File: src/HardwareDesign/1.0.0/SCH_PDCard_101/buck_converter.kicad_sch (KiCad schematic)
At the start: 43 parts, among them IC1 TPS552882QRPMRQ1, IC4 SN74LVC1G97QDCKRQ1, IC5 SN74LVC1G97QDCKRQ1, T1 BSZ065N06, T2 BSZ065N06

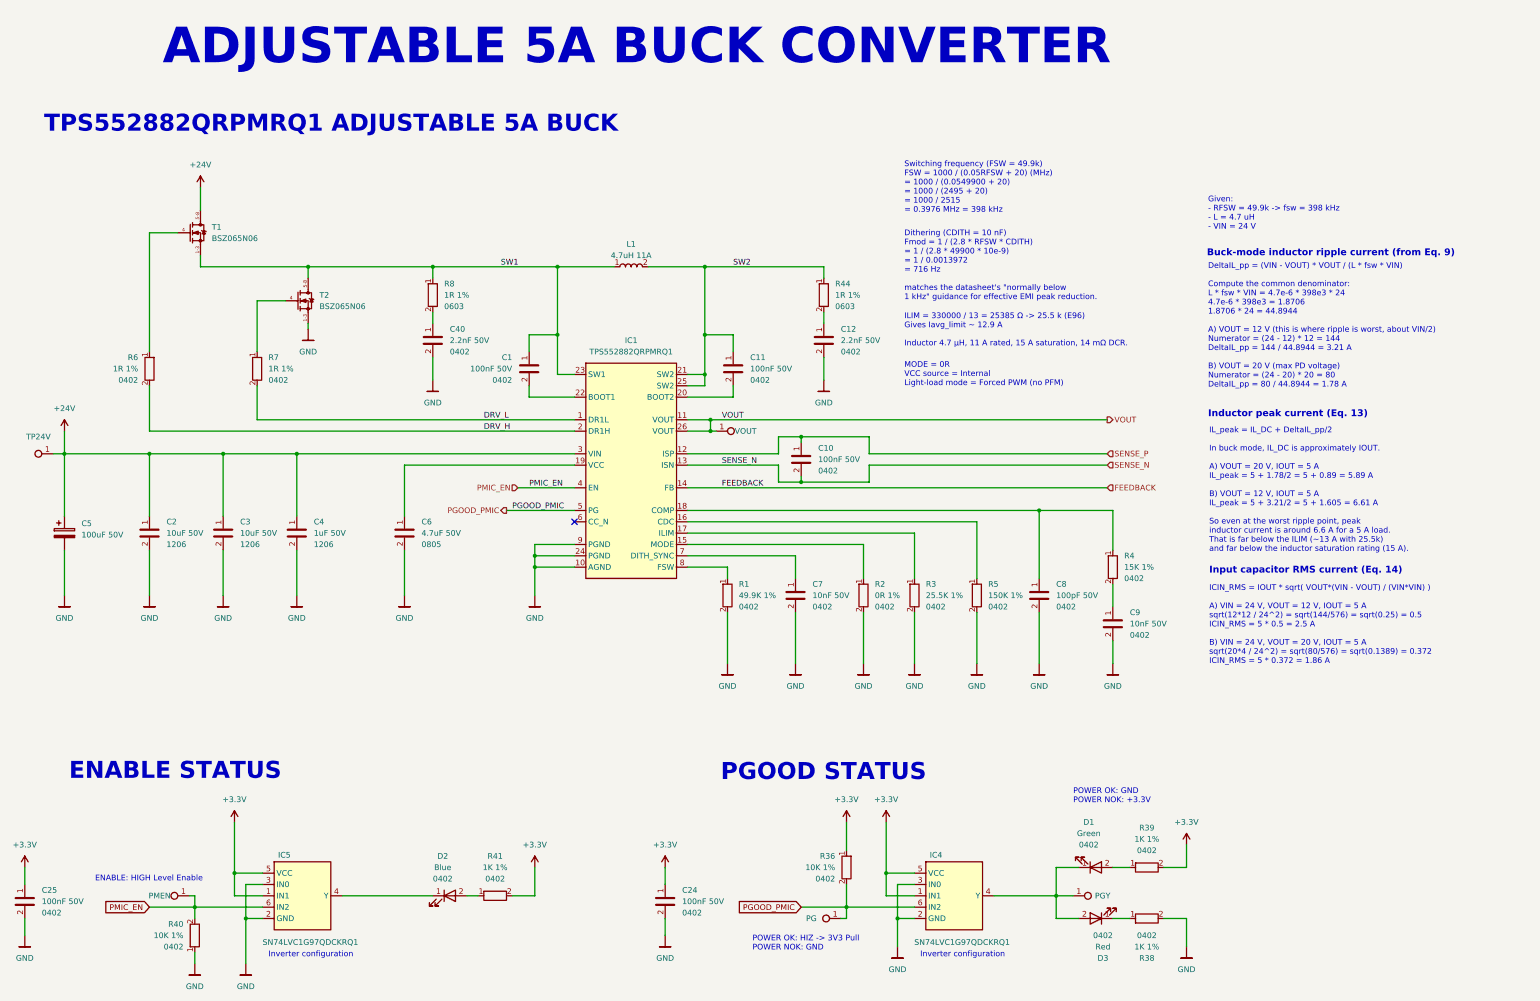
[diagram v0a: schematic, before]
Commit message: update component lib
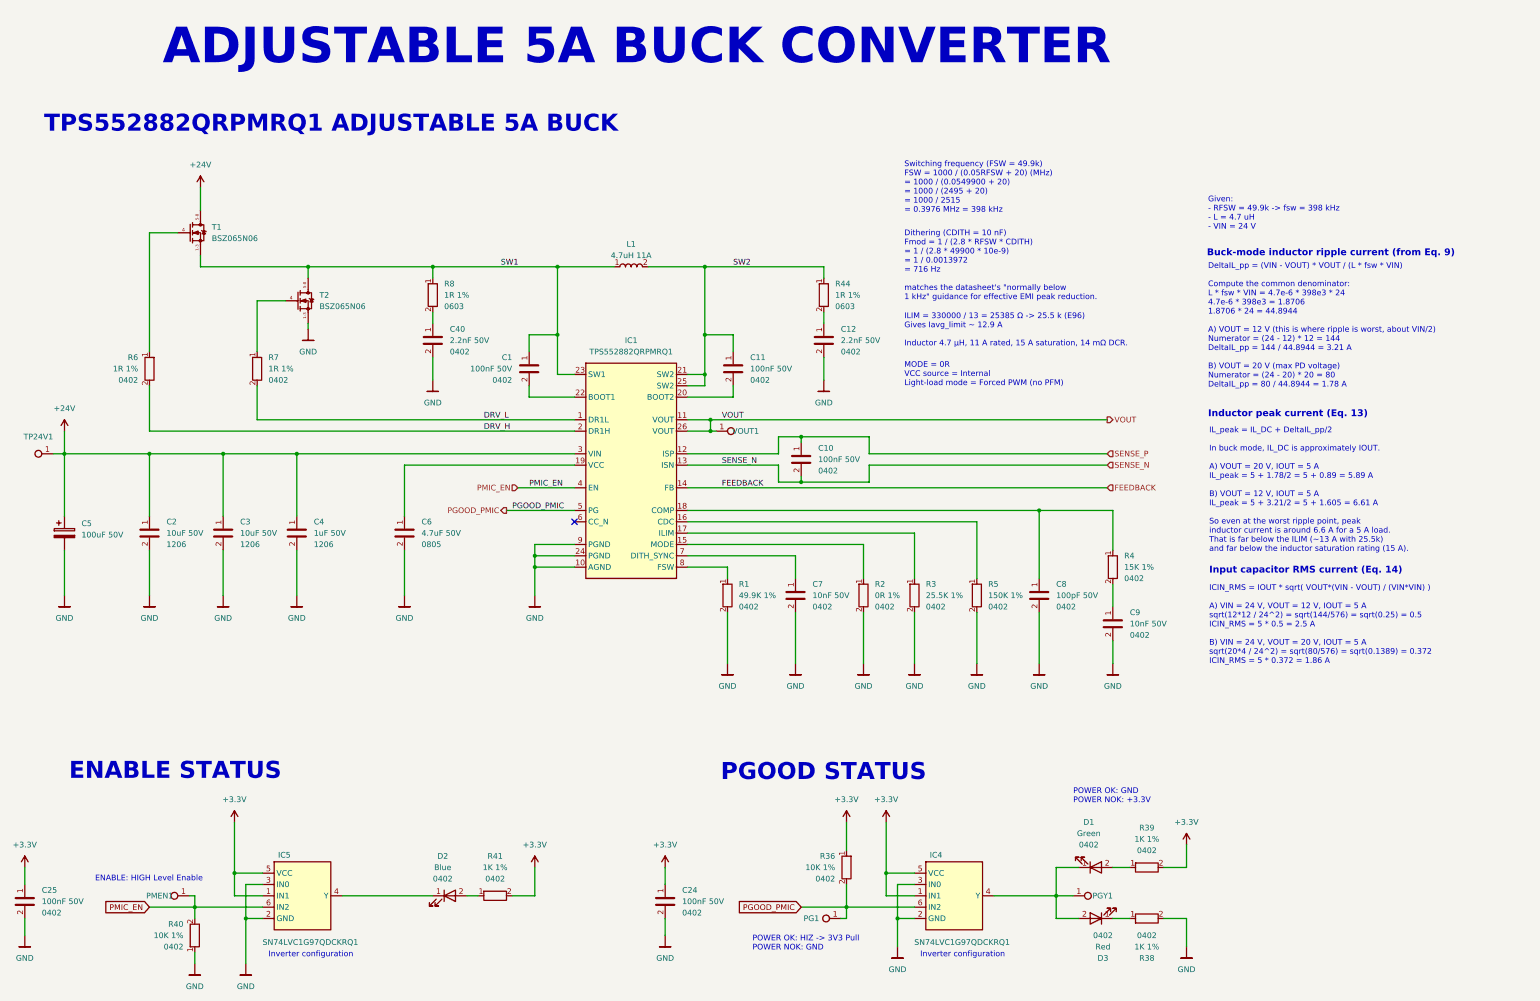
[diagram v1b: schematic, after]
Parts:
- C4: MFR (none) -> FH; MPN (none) -> 1206B105K500NT
- renumbered PG to PG1, PGY to PGY1, PMEN to PMEN1, TP24V to TP24V1, VOUT to VOUT1
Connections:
- net +24V: now also T1.5 (D), T1.6 (D), T1.7 (D), T1.8 (D); no longer T1.5-8
- net GND: now also T2.1 (S), T2.2 (S), T2.3 (S); no longer T2.1-3
- net SW1: now also T1.1 (S), T1.2 (S), T1.3 (S), T2.5 (D), T2.6 (D), T2.7 (D), T2.8 (D); no longer T1.1-3, T2.5-8
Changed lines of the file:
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@@
 		(on_board yes)
 		(dnp no)
-		(property "Reference" "VOUT"
+		(property "Reference" "VOUT1"
 			(at 235.204 109.22 90)
 			(effects
@@
 			(project "PDNode-600"
 				(path "/f9e05184-c88b-4a88-ae9c-ab2bdb32be7c/c5103ceb-5325-4a84-a025-9638a412984e/f06537ee-772d-44d3-8c50-e0ba41038c9c"
-					(reference "VOUT")
+					(reference "VOUT1")
 					(unit 1)
 				)
@@
 			)
 		)
-		(pin "5-8"
+		(pin "8"
 		)
-		(pin "1-3"
+		(pin "6"
 		)
 		(pin "4"
 		)
+		(pin "7"
+		)
+		(pin "2"
+		)
+		(pin "5"
+		)
+		(pin "1"
+		)
+		(pin "3"
+		)
 		(instances
 			(project ""
@@
 			)
 		)
-		(property "Datasheet" ""
+		(property "Datasheet" "https://jlcpcb.com/api/file/downloadByFileSystemAccessId/8588919304821202944"
 			(at 138.43 140.208 0)
 			(show_name yes)
@@
 			)
 		)
-		(property "Description" "50V 1uF X7R ±10% 1206 Multilayer Ceramic Capacitors MLCC - SMD/SMT ROHS"
+		(property "Description" "1uF 50V X7R ±10% 1206 Multilayer Ceramic Capacitors MLCC - SMD/SMT ROHS"
 			(at 138.43 144.272 0)
 			(show_name yes)
@@
 			)
 		)
-		(property "MFR" ""
+		(property "MFR" "FH "
 			(at 138.43 142.24 0)
 			(show_name yes)
@@
 			)
 		)
+		(property "MPN" "1206B105K500NT"
+			(at 138.43 148.336 0)
+			(effects
+				(font
+					(size 1.27 1.27)
+				)
+				(justify left)
+				(hide yes)
+			)
+		)
 		(pin "1"
 		)
@@
 		(pin "4"
 		)
-		(pin "5-8"
+		(pin "1"
+		)
+		(pin "7"
 		)
-		(pin "1-3"
+		(pin "5"
+		)
+		(pin "2"
+		)
+		(pin "6"
+		)
+		(pin "8"
+		)
+		(pin "3"
 		)
 		(instances
@@
 		(on_board yes)
 		(dnp no)
-		(property "Reference" "PGY"
+		(property "Reference" "PGY1"
 			(at 315.214 213.36 90)
 			(effects
@@
 			(project "PDNode-600"
 				(path "/f9e05184-c88b-4a88-ae9c-ab2bdb32be7c/c5103ceb-5325-4a84-a025-9638a412984e/f06537ee-772d-44d3-8c50-e0ba41038c9c"
-					(reference "PGY")
+					(reference "PGY1")
 					(unit 1)
 				)
@@
 		(on_board yes)
 		(dnp no)
-		(property "Reference" "PMEN"
+		(property "Reference" "PMEN1"
 			(at 103.886 213.36 90)
 			(effects
@@
 			(project "PDNode-600"
 				(path "/f9e05184-c88b-4a88-ae9c-ab2bdb32be7c/c5103ceb-5325-4a84-a025-9638a412984e/f06537ee-772d-44d3-8c50-e0ba41038c9c"
-					(reference "PMEN")
+					(reference "PMEN1")
 					(unit 1)
 				)
@@
 		(dnp no)
 		(fields_autoplaced yes)
-		(property "Reference" "TP24V"
+		(property "Reference" "TP24V1"
 			(at 76.708 110.49 90)
 			(effects
@@
 			(project ""
 				(path "/f9e05184-c88b-4a88-ae9c-ab2bdb32be7c/c5103ceb-5325-4a84-a025-9638a412984e/f06537ee-772d-44d3-8c50-e0ba41038c9c"
-					(reference "TP24V")
+					(reference "TP24V1")
 					(unit 1)
 				)
@@
 		(on_board yes)
 		(dnp no)
-		(property "Reference" "PG"
+		(property "Reference" "PG1"
 			(at 249.936 218.44 90)
 			(effects
@@
 			(project "PDNode-600"
 				(path "/f9e05184-c88b-4a88-ae9c-ab2bdb32be7c/c5103ceb-5325-4a84-a025-9638a412984e/f06537ee-772d-44d3-8c50-e0ba41038c9c"
-					(reference "PG")
+					(reference "PG1")
 					(unit 1)
 				)
